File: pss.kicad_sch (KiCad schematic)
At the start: 0 parts

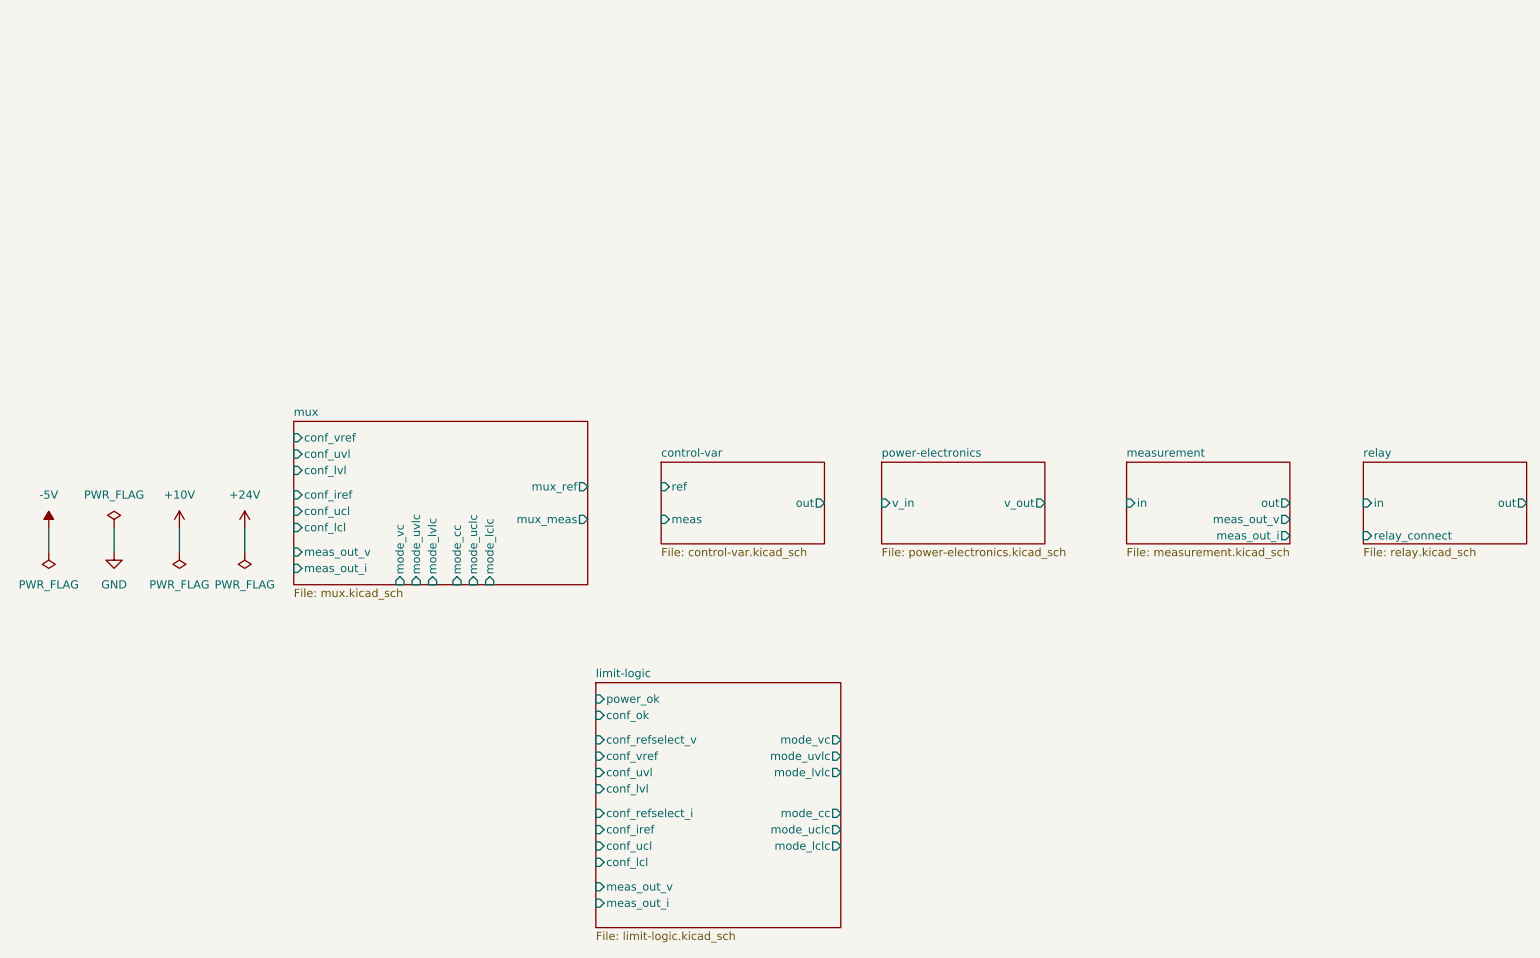
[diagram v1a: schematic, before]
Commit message: add conf digital to analog converter ad5672r to sub circuit
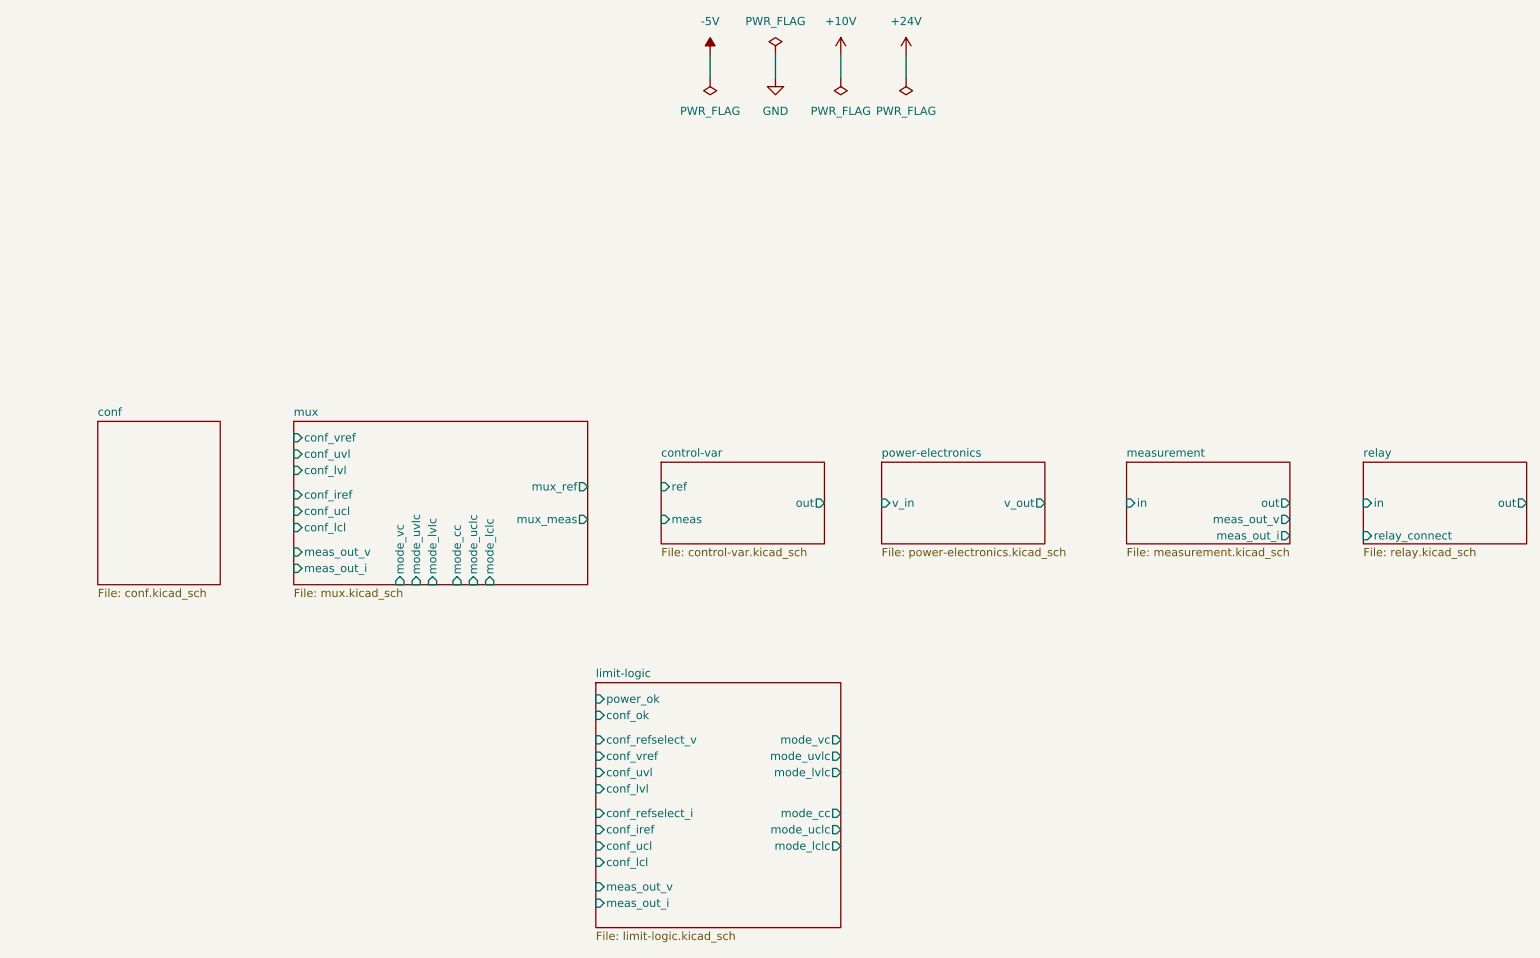
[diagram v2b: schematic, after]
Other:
- added sheet conf (conf.kicad_sch)
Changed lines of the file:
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@@
 	(wire
 		(pts
-			(xy 36.83 107.95) (xy 36.83 111.76)
+			(xy 139.7 34.29) (xy 139.7 38.1)
 		)
 		(stroke
@@
 	(wire
 		(pts
-			(xy 26.67 107.95) (xy 26.67 111.76)
+			(xy 129.54 34.29) (xy 129.54 38.1)
 		)
 		(stroke
@@
 	(wire
 		(pts
-			(xy 46.99 107.95) (xy 46.99 111.76)
+			(xy 149.86 34.29) (xy 149.86 38.1)
 		)
 		(stroke
@@
 	(wire
 		(pts
-			(xy 57.15 107.95) (xy 57.15 111.76)
+			(xy 160.02 34.29) (xy 160.02 38.1)
 		)
 		(stroke
@@
 	(symbol
 		(lib_id "pss:+10V")
-		(at 46.99 107.95 0)
+		(at 149.86 34.29 0)
 		(unit 1)
 		(exclude_from_sim no)
@@
 		(fields_autoplaced yes)
 		(property "Reference" "#PWR01002"
-			(at 46.99 111.76 0)
+			(at 149.86 38.1 0)
 			(effects
 				(font
@@
 		)
 		(property "Value" "+10V"
-			(at 46.99 102.87 0)
+			(at 149.86 29.21 0)
 			(effects
 				(font
@@
 		)
 		(property "Footprint" ""
-			(at 46.99 107.95 0)
+			(at 149.86 34.29 0)
 			(effects
 				(font
@@
 		)
 		(property "Datasheet" ""
-			(at 46.99 107.95 0)
+			(at 149.86 34.29 0)
 			(effects
 				(font
@@
 		)
 		(property "Description" "Power symbol creates a global label with name \"+10V\""
-			(at 46.99 107.95 0)
+			(at 149.86 34.29 0)
 			(effects
 				(font
@@
 	(symbol
 		(lib_id "pss:GND")
-		(at 36.83 111.76 0)
+		(at 139.7 38.1 0)
 		(unit 1)
 		(exclude_from_sim no)
@@
 		(fields_autoplaced yes)
 		(property "Reference" "#PWR01004"
-			(at 36.83 118.11 0)
+			(at 139.7 44.45 0)
 			(effects
 				(font
@@
 		)
 		(property "Value" "GND"
-			(at 36.83 116.84 0)
+			(at 139.7 43.18 0)
 			(effects
 				(font
@@
 		)
 		(property "Footprint" ""
-			(at 36.83 111.76 0)
+			(at 139.7 38.1 0)
 			(effects
 				(font
@@
 		)
 		(property "Datasheet" ""
-			(at 36.83 111.76 0)
+			(at 139.7 38.1 0)
 			(effects
 				(font
@@
 		)
 		(property "Description" "Power symbol creates a global label with name \"GND\" , ground"
-			(at 36.83 111.76 0)
+			(at 139.7 38.1 0)
 			(effects
 				(font
@@
 	(symbol
 		(lib_id "pss:+24V")
-		(at 57.15 107.95 0)
+		(at 160.02 34.29 0)
 		(unit 1)
 		(exclude_from_sim no)
@@
 		(fields_autoplaced yes)
 		(property "Reference" "#PWR01003"
-			(at 57.15 111.76 0)
+			(at 160.02 38.1 0)
 			(effects
 				(font
@@
 		)
 		(property "Value" "+24V"
-			(at 57.15 102.87 0)
+			(at 160.02 29.21 0)
 			(effects
 				(font
@@
 		)
 		(property "Footprint" ""
-			(at 57.15 107.95 0)
+			(at 160.02 34.29 0)
 			(effects
 				(font
@@
 		)
 		(property "Datasheet" ""
-			(at 57.15 107.95 0)
+			(at 160.02 34.29 0)
 			(effects
 				(font
@@
 		)
 		(property "Description" "Power symbol creates a global label with name \"+24V\""
-			(at 57.15 107.95 0)
+			(at 160.02 34.29 0)
 			(effects
 				(font
@@
 	(symbol
 		(lib_id "pss:PWR_FLAG")
-		(at 36.83 107.95 0)
+		(at 139.7 34.29 0)
 		(unit 1)
 		(exclude_from_sim no)
@@
 		(fields_autoplaced yes)
 		(property "Reference" "#FLG01004"
-			(at 36.83 106.045 0)
+			(at 139.7 32.385 0)
 			(effects
 				(font
@@
 		)
 		(property "Value" "PWR_FLAG"
-			(at 36.83 102.87 0)
+			(at 139.7 29.21 0)
 			(effects
 				(font
@@
 		)
 		(property "Footprint" ""
-			(at 36.83 107.95 0)
+			(at 139.7 34.29 0)
 			(effects
 				(font
@@
 		)
 		(property "Datasheet" "~"
-			(at 36.83 107.95 0)
+			(at 139.7 34.29 0)
 			(effects
 				(font
@@
 		)
 		(property "Description" "Special symbol for telling ERC where power comes from"
-			(at 36.83 107.95 0)
+			(at 139.7 34.29 0)
 			(effects
 				(font
@@
 	(symbol
 		(lib_id "pss:PWR_FLAG")
-		(at 57.15 111.76 180)
+		(at 160.02 38.1 180)
 		(unit 1)
 		(exclude_from_sim no)
@@
 		(fields_autoplaced yes)
 		(property "Reference" "#FLG01003"
-			(at 57.15 113.665 0)
+			(at 160.02 40.005 0)
 			(effects
 				(font
@@
 		)
 		(property "Value" "PWR_FLAG"
-			(at 57.15 116.84 0)
+			(at 160.02 43.18 0)
 			(effects
 				(font
@@
 		)
 		(property "Footprint" ""
-			(at 57.15 111.76 0)
+			(at 160.02 38.1 0)
 			(effects
 				(font
@@
 		)
 		(property "Datasheet" "~"
-			(at 57.15 111.76 0)
+			(at 160.02 38.1 0)
 			(effects
 				(font
@@
 		)
 		(property "Description" "Special symbol for telling ERC where power comes from"
-			(at 57.15 111.76 0)
+			(at 160.02 38.1 0)
 			(effects
 				(font
@@
 	(symbol
 		(lib_id "pss:-5V")
-		(at 26.67 107.95 0)
+		(at 129.54 34.29 0)
 		(unit 1)
 		(exclude_from_sim no)
@@
 		(fields_autoplaced yes)
 		(property "Reference" "#PWR01001"
-			(at 26.67 111.76 0)
+			(at 129.54 38.1 0)
 			(effects
 				(font
@@
 		)
 		(property "Value" "-5V"
-			(at 26.67 102.87 0)
+			(at 129.54 29.21 0)
 			(effects
 				(font
@@
 		)
 		(property "Footprint" ""
-			(at 26.67 107.95 0)
+			(at 129.54 34.29 0)
 			(effects
 				(font
@@
 		)
 		(property "Datasheet" ""
-			(at 26.67 107.95 0)
+			(at 129.54 34.29 0)
 			(effects
 				(font
@@
 		)
 		(property "Description" "Power symbol creates a global label with name \"-5V\""
-			(at 26.67 107.95 0)
+			(at 129.54 34.29 0)
 			(effects
 				(font
@@
 	(symbol
 		(lib_id "pss:PWR_FLAG")
-		(at 26.67 111.76 180)
+		(at 129.54 38.1 180)
 		(unit 1)
 		(exclude_from_sim no)
@@
 		(fields_autoplaced yes)
 		(property "Reference" "#FLG01001"
-			(at 26.67 113.665 0)
+			(at 129.54 40.005 0)
 			(effects
 				(font
@@
 		)
 		(property "Value" "PWR_FLAG"
-			(at 26.67 116.84 0)
+			(at 129.54 43.18 0)
 			(effects
 				(font
@@
 		)
 		(property "Footprint" ""
-			(at 26.67 111.76 0)
+			(at 129.54 38.1 0)
 			(effects
 				(font
@@
 		)
 		(property "Datasheet" "~"
-			(at 26.67 111.76 0)
+			(at 129.54 38.1 0)
 			(effects
 				(font
@@
 		)
 		(property "Description" "Special symbol for telling ERC where power comes from"
-			(at 26.67 111.76 0)
+			(at 129.54 38.1 0)
 			(effects
 				(font
@@
 	(symbol
 		(lib_id "pss:PWR_FLAG")
-		(at 46.99 111.76 180)
+		(at 149.86 38.1 180)
 		(unit 1)
 		(exclude_from_sim no)
@@
 		(fields_autoplaced yes)
 		(property "Reference" "#FLG01002"
-			(at 46.99 113.665 0)
+			(at 149.86 40.005 0)
 			(effects
 				(font
@@
 		)
 		(property "Value" "PWR_FLAG"
-			(at 46.99 116.84 0)
+			(at 149.86 43.18 0)
 			(effects
 				(font
@@
 		)
 		(property "Footprint" ""
-			(at 46.99 111.76 0)
+			(at 149.86 38.1 0)
 			(effects
 				(font
@@
 		)
 		(property "Datasheet" "~"
-			(at 46.99 111.76 0)
+			(at 149.86 38.1 0)
 			(effects
 				(font
@@
 		)
 		(property "Description" "Special symbol for telling ERC where power comes from"
-			(at 46.99 111.76 0)
+			(at 149.86 38.1 0)
 			(effects
 				(font
@@
 				)
 			)
+		)
+	)
+	(sheet
+		(at 34.29 91.44)
+		(size 19.05 25.4)
+		(fields_autoplaced yes)
+		(stroke
+			(width 0.1524)
+			(type solid)
+		)
+		(fill
+			(color 0 0 0 0.0000)
+		)
+		(property "Sheetname" "conf"
+			(at 34.29 90.7284 0)
+			(effects
+				(font
+					(size 1.27 1.27)
+				)
+				(justify left bottom)
+			)
+		)
+		(property "Sheetfile" "conf.kicad_sch"
+			(at 34.29 117.4246 0)
+			(effects
+				(font
+					(size 1.27 1.27)
+				)
+				(justify left top)
+			)
+		)
+		(instances
+			(project "pss"
+				(path "/3c438cf7-9350-4e9f-8115-1deba8984176"
+					(page "29")
+				)
+			)

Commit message: add conf hierarchical spi input
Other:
- sheet conf ports: added SDI, SDO, ~{CS}, ~{SCLK}; removed none
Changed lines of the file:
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@@
+			)
+		)
+		(pin "SDO" output
+			(at 34.29 101.6 180)
+			(effects
+				(font
+					(size 1.27 1.27)
+				)
+				(justify left)
+			)
+		)
+		(pin "~{SCLK}" input
+			(at 34.29 96.52 180)
+			(effects
+				(font
+					(size 1.27 1.27)
+				)
+				(justify left)
+			)
+		)
+		(pin "SDI" input
+			(at 34.29 99.06 180)
+			(effects
+				(font
+					(size 1.27 1.27)
+				)
+				(justify left)
+			)
+		)
+		(pin "~{CS}" input
+			(at 34.29 93.98 180)
+			(effects
+				(font
+					(size 1.27 1.27)
+				)
+				(justify left)
 			)
 		)

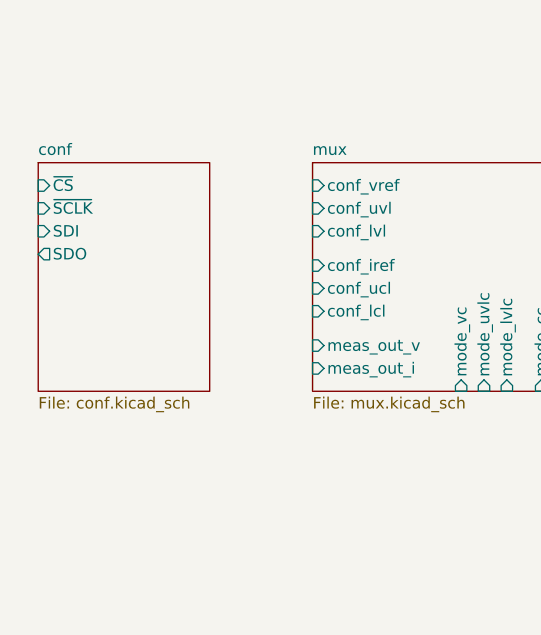
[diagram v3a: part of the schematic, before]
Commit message: add conf hierarchical pins
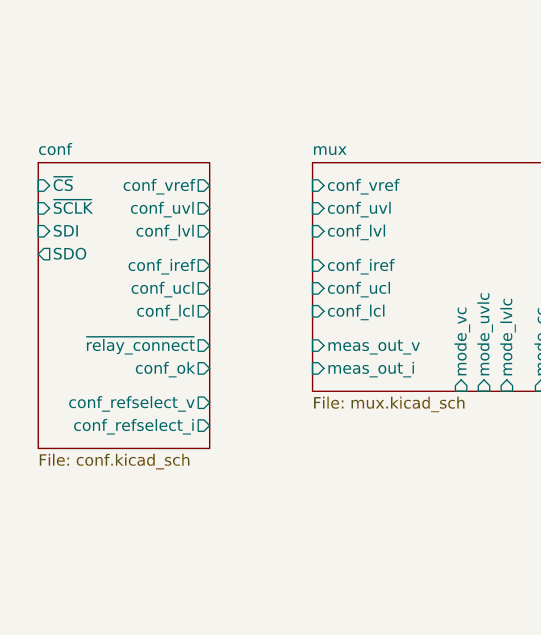
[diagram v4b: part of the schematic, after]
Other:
- sheet conf ports: added conf_iref, conf_lcl, conf_lvl, conf_ok, conf_refselect_i, conf_refselect_v, conf_ucl, conf_uvl, conf_vref, ~{relay_connect}; removed none
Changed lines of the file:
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@@
 	(sheet
 		(at 34.29 91.44)
-		(size 19.05 25.4)
+		(size 19.05 31.75)
 		(fields_autoplaced yes)
 		(stroke
@@
 		)
 		(property "Sheetfile" "conf.kicad_sch"
-			(at 34.29 117.4246 0)
+			(at 34.29 123.7746 0)
 			(effects
 				(font
@@
 			)
 		)
+		(pin "conf_ok" output
+			(at 53.34 114.3 0)
+			(effects
+				(font
+					(size 1.27 1.27)
+				)
+				(justify right)
+			)
+		)
+		(pin "~{relay_connect}" output
+			(at 53.34 111.76 0)
+			(effects
+				(font
+					(size 1.27 1.27)
+				)
+				(justify right)
+			)
+		)
+		(pin "conf_lvl" output
+			(at 53.34 99.06 0)
+			(effects
+				(font
+					(size 1.27 1.27)
+				)
+				(justify right)
+			)
+		)
+		(pin "conf_ucl" output
+			(at 53.34 105.41 0)
+			(effects
+				(font
+					(size 1.27 1.27)
+				)
+				(justify right)
+			)
+		)
+		(pin "conf_lcl" output
+			(at 53.34 107.95 0)
+			(effects
+				(font
+					(size 1.27 1.27)
+				)
+				(justify right)
+			)
+		)
+		(pin "conf_uvl" output
+			(at 53.34 96.52 0)
+			(effects
+				(font
+					(size 1.27 1.27)
+				)
+				(justify right)
+			)
+		)
+		(pin "conf_iref" output
+			(at 53.34 102.87 0)
+			(effects
+				(font
+					(size 1.27 1.27)
+				)
+				(justify right)
+			)
+		)
+		(pin "conf_vref" output
+			(at 53.34 93.98 0)
+			(effects
+				(font
+					(size 1.27 1.27)
+				)
+				(justify right)
+			)
+		)
+		(pin "conf_refselect_i" output
+			(at 53.34 120.65 0)
+			(effects
+				(font
+					(size 1.27 1.27)
+				)
+				(justify right)
+			)
+		)
+		(pin "conf_refselect_v" output
+			(at 53.34 118.11 0)
+			(effects
+				(font
+					(size 1.27 1.27)
+				)
+				(justify right)
+			)
+		)

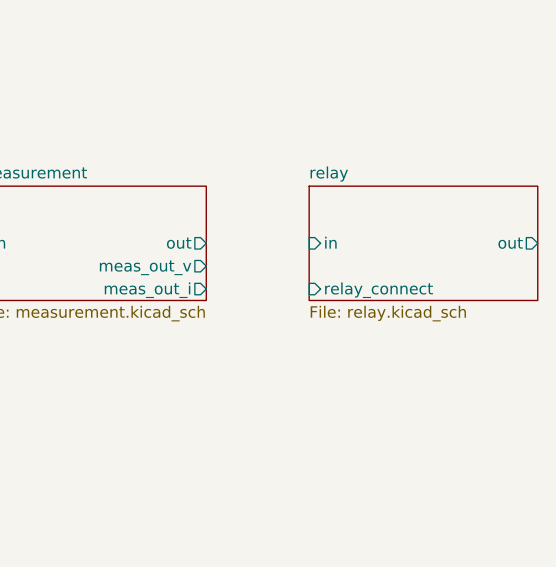
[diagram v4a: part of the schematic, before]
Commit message: edit relay invert input logic
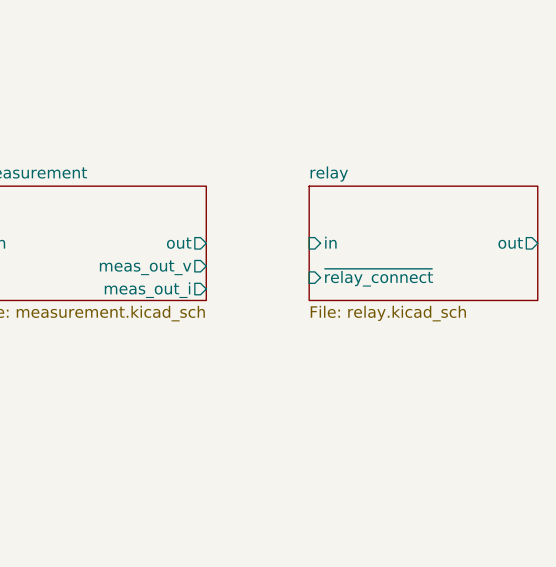
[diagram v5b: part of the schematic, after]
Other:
- sheet relay ports: added ~{relay_connect}; removed relay_connect
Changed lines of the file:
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@@
 			)
 		)
-		(pin "relay_connect" input
-			(at 231.14 109.22 180)
+		(pin "~{relay_connect}" input
+			(at 231.14 107.95 180)
 			(effects
 				(font
